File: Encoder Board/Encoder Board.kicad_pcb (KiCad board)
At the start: 2 copper layers, 16 parts, among them J1 Conn_02x05_Odd_Even, J2 Conn_02x05_Odd_Even, J3 Conn_01x02_Pin, U1 AM26LV32xD, U2 AM26LV31xD_1

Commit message: Layout
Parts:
- J3: footprint Connector_PinHeader_1.00mm:PinHeader_1x02_P1.00mm_Horizontal -> Connector_PinHeader_2.00mm:PinHeader_1x02_P2.00mm_Vertical
- moved C1 60.5 mm to (90.8, 48.0)
- moved GND_1 45.0 mm to (84.2, 82.8)
- moved +5V_1 43.4 mm to (88.6, 67.0)
- moved NT1 39.3 mm to (118.2, 59.4), turned to 180 degrees
- moved J2 26.7 mm to (125.7, 56.0)
- moved J3 26.4 mm to (126.0, 73.8), turned to 180 degrees
- moved U2 25.7 mm to (124.5, 83.6), turned to 0 degrees
- moved J1 21.5 mm to (81.7, 69.2)
- moved C2 13.6 mm to (129.6, 80.4), turned to -90 degrees
- moved +3V3_1 12.9 mm to (122.2, 67.6)
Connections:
- R1 pad 1: /B_N -> /A_N
- R1 pad 2: /B -> /A
- R2 pad 1: /A_N -> /B_N
- R2 pad 2: /A -> /B
- U1 pad 1: /B_N -> /A_N
- U1 pad 2: /B -> /A
- U1 pad 6: /A -> /B
- U1 pad 7: /A_N -> /B_N
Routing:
- net +3V3: track 0.00 -> 85.9 mm, vias 0 -> 2
- net /A_N: track 8.81 -> 86.1 mm, vias 0 -> 2
- net +5V: track 0.00 -> 65.9 mm, vias 0 -> 2
- net /A: track 13.3 -> 76.8 mm, vias 0 -> 2
- net /B_N: track 10.5 -> 68.6 mm, vias 0 -> 2
- net /INDEX_N: track 23.8 -> 81.0 mm, vias 0 -> 2
- net /INDEX: track 32.5 -> 87.0 mm, vias 0 -> 2
- net /B: track 14.9 -> 67.0 mm, vias 0 -> 2
- net /B_3V3: track 0.00 -> 14.5 mm
- net /A_3V3: track 0.00 -> 14.5 mm
- net GND: track 0.00 -> 13.7 mm, vias 0 -> 4
- net /TRIGGER_P: track 0.00 -> 12.0 mm
- net /TRIGGER_N: track 0.00 -> 10.7 mm
- net /INDEX_3V3: track 0.00 -> 9.39 mm
- net /TRIGGER: track 0.00 -> 8.46 mm
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- added copper zone on B.Cu, net GND
- added copper zone on F.Cu, net GND
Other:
- board outline added: 56.8 x 55.6 mm

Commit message: Update 2x5 connector footprint
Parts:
- J1, J2: footprint Connector_Molex_Milligrid:Molex_8783210xx_2x05_P2.0mm_Header_Vertical -> Connector_PinHeader_2.54mm:PinHeader_2x05_P2.54mm_Vertical
- moved J2 5.70 mm to (127.9, 61.3), turned to 180 degrees
- moved J1 4.36 mm to (83.9, 73.0), turned to 180 degrees
- moved +5V_1 1.61 mm to (88.4, 65.4)
- moved GND_1 0.45 mm to (83.8, 82.6)
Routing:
- net GND: track 13.7 -> 9.45 mm, vias 4 -> 2
- net /A_N: track 86.1 -> 83.1 mm, vias 2 -> 0
- net /INDEX: track 87.0 -> 84.3 mm, vias 2 -> 0
- net +5V: track 65.9 -> 63.3 mm, vias 2 -> 1
- net /B_N: track 68.6 -> 66.3 mm, vias 2 -> 0
- net /INDEX_N: track 81.0 -> 78.9 mm, vias 2 -> 0
- net /B: track 67.0 -> 66.5 mm, vias 2 -> 0
- net /A: track 76.8 -> 76.7 mm, vias 2 -> 0

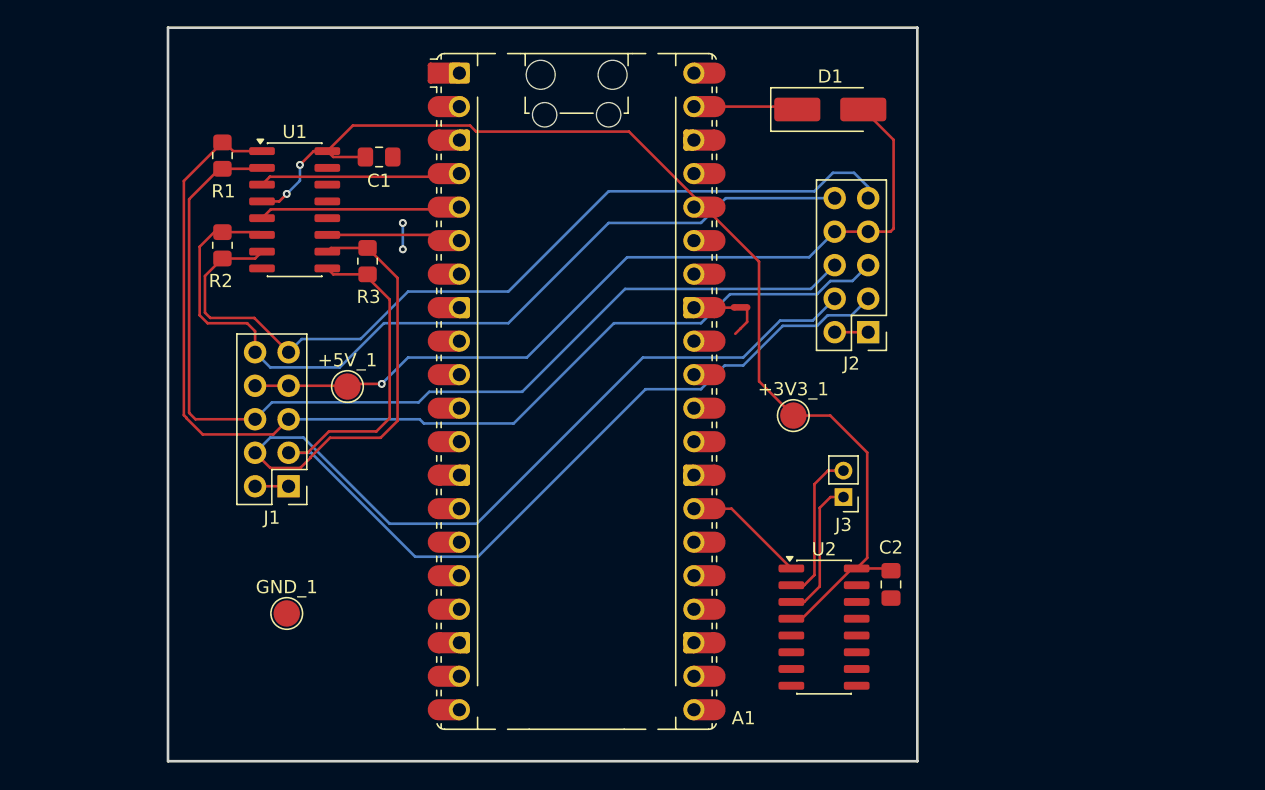
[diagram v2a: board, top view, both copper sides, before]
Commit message: Update layout with new passives
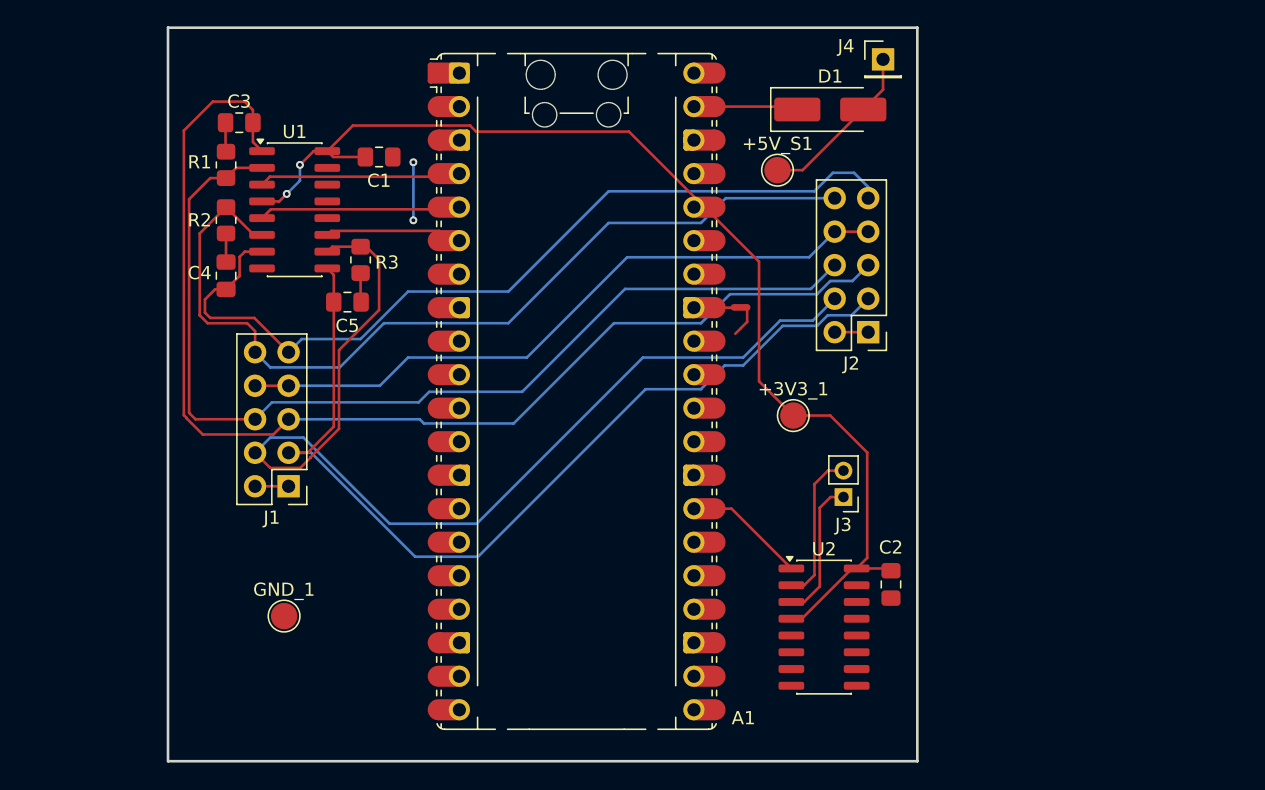
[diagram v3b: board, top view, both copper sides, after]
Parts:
- added C3: 0.0047mF, Capacitor_SMD:C_0805_2012Metric_Pad1.18x1.45mm_HandSolder, F.Cu at (80.2, 45.4)
- added C4: 0.0047mF, Capacitor_SMD:C_0805_2012Metric_Pad1.18x1.45mm_HandSolder, F.Cu at (79.2, 57.0)
- added C5: 0.0047mF, Capacitor_SMD:C_0805_2012Metric_Pad1.18x1.45mm_HandSolder, F.Cu at (88.4, 59.0)
- added J4: Conn_01x01_Pin, Connector_PinHeader_2.54mm:PinHeader_1x01_P2.54mm_Vertical, F.Cu at (129.0, 40.6)
- R1, R2, R3: value 120 -> 110
- moved +5V_S1 36.5 mm to (121.0, 49.0)
- moved R2 1.91 mm to (79.2, 52.8)
- moved R1 0.76 mm to (79.2, 48.6)
- moved R3 0.53 mm to (89.4, 55.8)
- moved GND_1 0.28 mm to (83.6, 82.8)
- renumbered +5V_1 to +5V_S1
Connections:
- +5V_S1 pad 1: +5V -> +5V_S
- D1 pad 2: +5V -> +5V_S
- J1 pad 7: +5V -> +5V_E
- J1 pad 8: +5V -> +5V_E
- J2 pad 7: +5V -> +5V_E
- J2 pad 8: +5V -> +5V_E
- R1 pad 1: /A_N -> Net-(C3-Pad2)
- R2 pad 1: /B_N -> Net-(C4-Pad2)
- R3 pad 1: /INDEX_N -> Net-(C5-Pad2)
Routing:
- net +5V: track 63.3 -> 0.00 mm, vias 1 -> 0
- net +5V_E: track 0.00 -> 51.3 mm
- net +5V_S: track 0.00 -> 12.8 mm
- net /INDEX_N: track 78.9 -> 71.7 mm
- net /A_N: track 83.1 -> 90.2 mm
- net /INDEX: track 84.3 -> 80.8 mm
- net Net-(C5-Pad2): track 0.00 -> 2.45 mm
- net GND: track 9.45 -> 11.9 mm
- net Net-(C3-Pad2): track 0.00 -> 2.27 mm
- net Net-(C4-Pad2): track 0.00 -> 2.16 mm
- net /B: track 66.5 -> 68.6 mm

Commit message: remove differential trigger
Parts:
- removed C2: 0.1u, Capacitor_SMD:C_0805_2012Metric_Pad1.18x1.45mm_HandSolder
- removed U2: AM26LV31xD_1, Package_SO:SOIC-16_3.9x9.9mm_P1.27mm
- J3: value Conn_01x02_Pin -> Conn_01x01_Pin; footprint Connector_PinHeader_2.00mm:PinHeader_1x02_P2.00mm_Vertical -> Connector_PinHeader_2.54mm:PinHeader_1x01_P2.54mm_Vertical
- moved +3V3_1 39.9 mm to (89.2, 45.2)
- moved J3 2.54 mm to (128.4, 74.6), turned to 0 degrees
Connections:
- J3 pad 1: /TRIGGER_N -> /TRIGGER
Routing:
- net +3V3: track 85.9 -> 42.0 mm
- net /TRIGGER_P: track 12.0 -> 0.00 mm
- net /TRIGGER_N: track 10.7 -> 0.00 mm
- net /TRIGGER: track 8.46 -> 13.0 mm

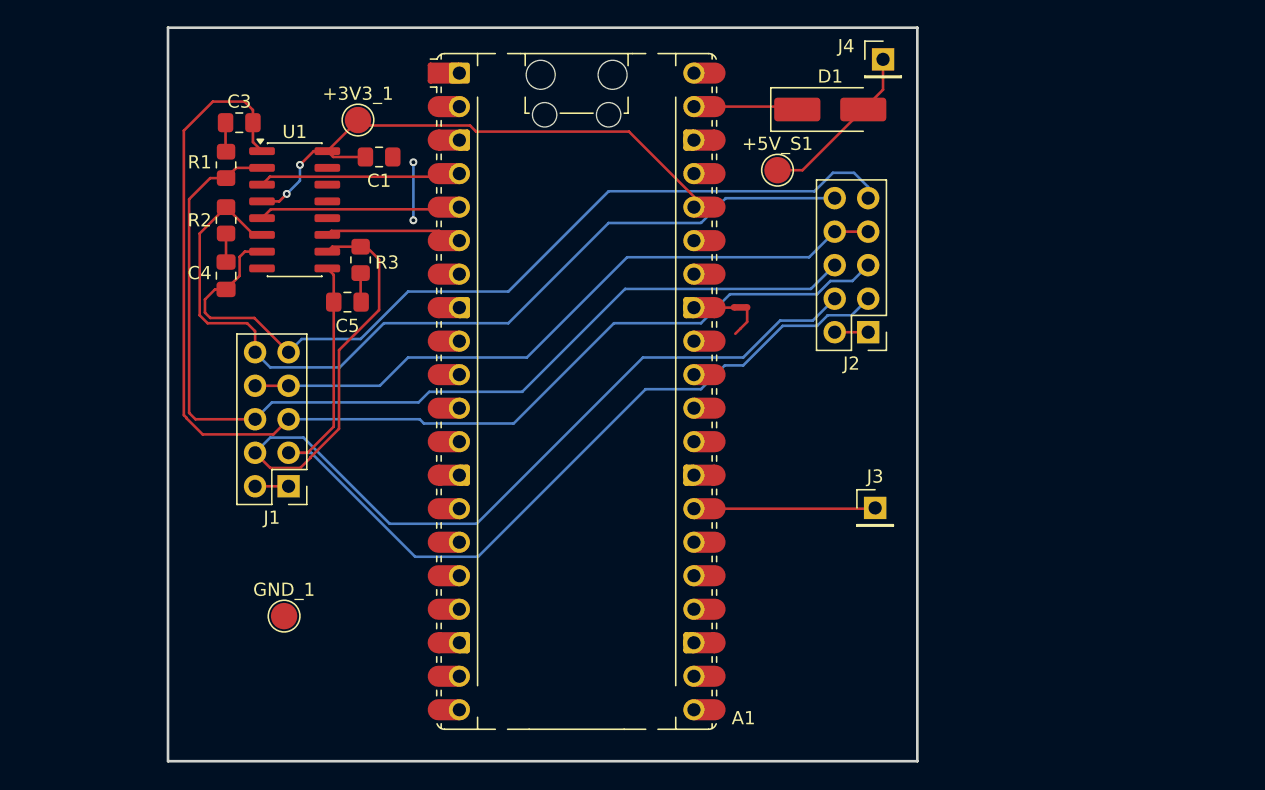
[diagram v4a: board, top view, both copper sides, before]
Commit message: Place & route components to optimize board size
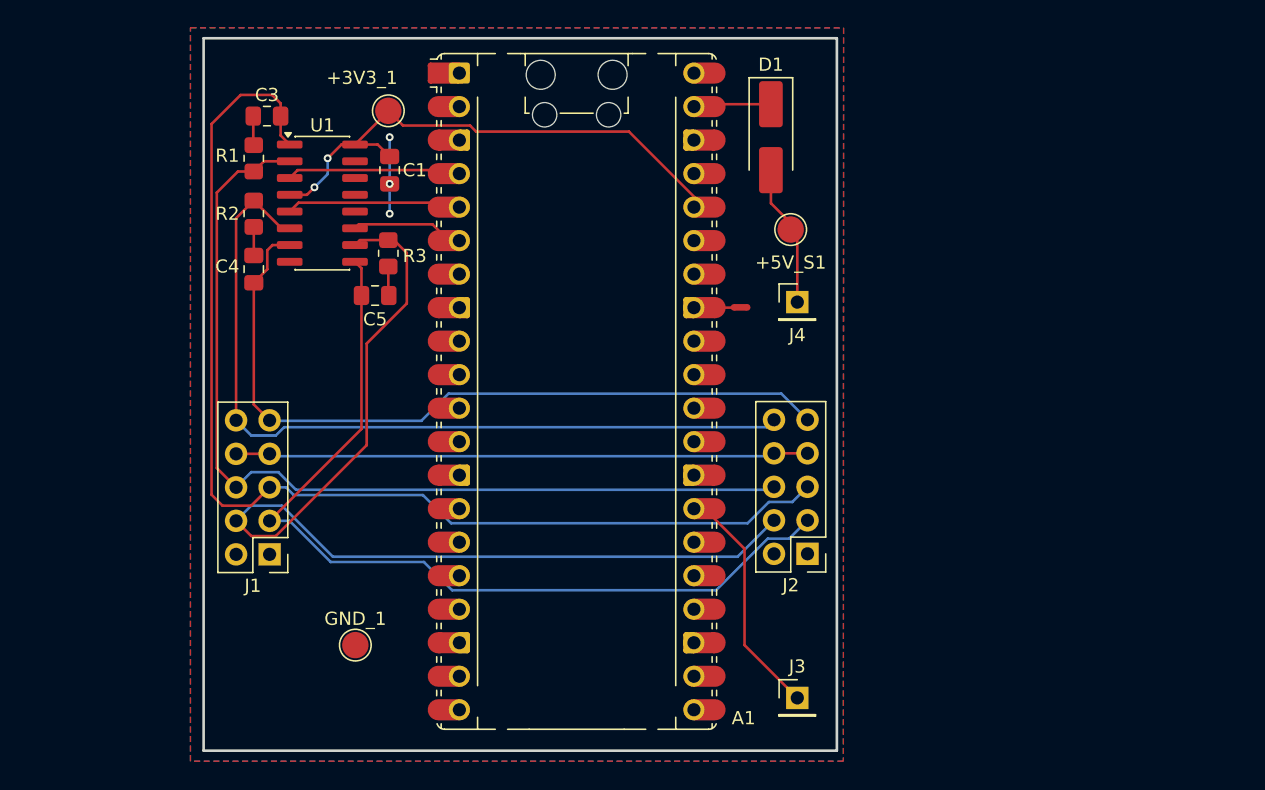
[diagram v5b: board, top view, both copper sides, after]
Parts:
- moved J4 19.5 mm to (122.5, 59.0)
- moved J2 17.4 mm to (123.3, 78.1)
- moved J3 15.6 mm to (122.5, 89.0)
- moved GND_1 5.83 mm to (89.0, 85.0)
- moved J1 5.36 mm to (82.5, 78.1)
- moved D1 4.97 mm to (120.5, 46.5), turned to -90 degrees
- moved +5V_S1 4.61 mm to (122.0, 53.5)
- moved +3V3_1 2.40 mm to (91.5, 44.5)
- moved C3 2.16 mm to (82.3, 44.9)
- moved C4 2.16 mm to (81.3, 56.5)
- moved C5 2.16 mm to (90.5, 58.5)
- moved R1 2.16 mm to (81.3, 48.1)
- moved R2 2.16 mm to (81.3, 52.3)
- moved R3 2.16 mm to (91.5, 55.3)
- moved U1 2.16 mm to (86.5, 51.5)
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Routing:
- net +5V_E: track 51.3 -> 43.5 mm
- net /B_N: track 66.1 -> 58.4 mm
- net /B: track 68.6 -> 62.6 mm
- net GND: track 11.9 -> 5.80 mm, vias 2 -> 3
- net /A: track 76.8 -> 71.5 mm
- net /TRIGGER: track 13.0 -> 17.3 mm
- net /INDEX_N: track 71.7 -> 67.9 mm
- net /INDEX: track 80.8 -> 77.5 mm
- net /A_N: track 90.2 -> 87.0 mm
- net /A_3V3: track 14.5 -> 12.4 mm
- net +3V3: track 42.0 -> 40.0 mm
- net /B_3V3: track 14.5 -> 12.5 mm
- net Net-(A1-VSYS): track 7.13 -> 5.11 mm
- net +5V_S: track 12.8 -> 10.8 mm
- net /INDEX_3V3: track 9.64 -> 8.18 mm
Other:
- board size 56.8 x 55.6 mm -> 48 x 54 mm

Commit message: Update DRC from PCBWay
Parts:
- +3V3_1, +5V_S1, GND_1: footprint TestPoint:TestPoint_Pad_D2.0mm -> TestPoints_WideSM:TestPoint_Pad_D2.0mm_WideSM
- moved J4 1.00 mm to (122.5, 60.0)
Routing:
- net +5V_S: track 10.8 -> 11.8 mm
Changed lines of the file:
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@@
 		(0 "F.Cu" signal)
 		(2 "B.Cu" signal)
-		(9 "F.Adhes" user "F.Adhesive")
-		(11 "B.Adhes" user "B.Adhesive")
 		(13 "F.Paste" user)
 		(15 "B.Paste" user)
@@
 		(1 "F.Mask" user)
 		(3 "B.Mask" user)
-		(17 "Dwgs.User" user "User.Drawings")
-		(19 "Cmts.User" user "User.Comments")
-		(21 "Eco1.User" user "User.Eco1")
-		(23 "Eco2.User" user "User.Eco2")
 		(25 "Edge.Cuts" user)
 		(27 "Margin" user)
@@
 		(35 "F.Fab" user)
 		(33 "B.Fab" user)
-		(39 "User.1" user)
-		(41 "User.2" user)
-		(43 "User.3" user)
-		(45 "User.4" user)
 	)
 	(setup
+		(stackup
+			(layer "F.SilkS"
+				(type "Top Silk Screen")
+			)
+			(layer "F.Paste"
+				(type "Top Solder Paste")
+			)
+			(layer "F.Mask"
+				(type "Top Solder Mask")
+				(thickness 0.01)
+			)
+			(layer "F.Cu"
+				(type "copper")
+				(thickness 0.035)
+			)
+			(layer "dielectric 1"
+				(type "core")
+				(thickness 1.51)
+				(material "FR4")
+				(epsilon_r 4.5)
+				(loss_tangent 0.02)
+			)
+			(layer "B.Cu"
+				(type "copper")
+				(thickness 0.035)
+			)
+			(layer "B.Mask"
+				(type "Bottom Solder Mask")
+				(thickness 0.01)
+			)
+			(layer "B.Paste"
+				(type "Bottom Solder Paste")
+			)
+			(layer "B.SilkS"
+				(type "Bottom Silk Screen")
+			)
+			(copper_finish "None")
+			(dielectric_constraints no)
+		)
 		(pad_to_mask_clearance 0)
+		(solder_mask_min_width 0.1016)
 		(allow_soldermask_bridges_in_footprints no)
 		(tenting
@@
 	(footprint "Connector_PinHeader_2.54mm:PinHeader_1x01_P2.54mm_Vertical"
 		(layer "F.Cu")
-		(at 122.5 59)
+		(at 122.5 60)
 		(descr "Through hole straight pin header, 1x01, 2.54mm pitch, single row")
 		(tags "Through hole pin header THT 1x01 2.54mm single row")
@@
 		)
 	)
-	(footprint "TestPoint:TestPoint_Pad_D2.0mm"
+	(footprint "TestPoints_WideSM:TestPoint_Pad_D2.0mm_WideSM"
 		(layer "F.Cu")
 		(at 91.5 44.5)
@@
 		(tags "test point SMD pad")
 		(property "Reference" "+3V3_1"
-			(at -2 -2.5 0)
+			(at -1 -2.5 0)
 			(layer "F.SilkS")
 			(effects
@@
 		(fp_circle
 			(center 0 0)
-			(end 0 1.2)
+			(end 1.3 0)
 			(stroke
 				(width 0.12)
@@
 		)
 	)
-	(footprint "TestPoint:TestPoint_Pad_D2.0mm"
+	(footprint "TestPoints_WideSM:TestPoint_Pad_D2.0mm_WideSM"
 		(layer "F.Cu")
 		(at 89 85)
@@
 		(tags "test point SMD pad")
 		(property "Reference" "GND_1"
-			(at 0 -1.998 0)
+			(at 0 2.5 0)
 			(layer "F.SilkS")
 			(effects
@@
 		(fp_circle
 			(center 0 0)
-			(end 0 1.2)
+			(end 1.3 0)
 			(stroke
 				(width 0.12)
@@
 		(tags "capacitor handsolder")
 		(property "Reference" "C1"
-			(at 0 -1.9 180)
+			(at 2.5 0.1 180)
 			(layer "F.SilkS")
 			(effects
@@
 		)
 	)
-	(footprint "TestPoint:TestPoint_Pad_D2.0mm"
+	(footprint "TestPoints_WideSM:TestPoint_Pad_D2.0mm_WideSM"
 		(layer "F.Cu")
 		(at 122 53.5)
@@
 		(fp_circle
 			(center 0 0)
-			(end 0 1.2)
+			(end 1.3 0)
 			(stroke
 				(width 0.12)
@@
 	)
 	(segment
-		(start 122.5 59)
+		(start 122 53.5)
 		(end 122.5 54)
 		(width 0.2)
@@
 	)
 	(segment
-		(start 122.5 54)
-		(end 122 53.5)
+		(start 122 53.5)
+		(end 122 53)
 		(width 0.2)
 		(layer "F.Cu")
@@
 	)
 	(segment
-		(start 122 53.5)
-		(end 122 53)
+		(start 120.5 51.5)
+		(end 120.5 49)
 		(width 0.2)
 		(layer "F.Cu")
@@
 	)
 	(segment
-		(start 120.5 51.5)
-		(end 120.5 49)
+		(start 122.5 54)
+		(end 122.5 60)
 		(width 0.2)
 		(layer "F.Cu")
@@
 	)
 	(segment
-		(start 91.5 44.5)
-		(end 92.615 45.615)
+		(start 108.729779 46.079)
+		(end 108.733779 46.075)
+		(width 0.2)
+		(layer "F.Cu")
+		(net "+3V3")
+	)
+	(segment
+		(start 92.5 45.5)
+		(end 97.57918 45.5)
 		(width 0.2)
 		(layer "F.Cu")
@@
 	)
 	(segment
+		(start 103.883779 46.075)
+		(end 107.666221 46.075)
+		(width 0.2)
+		(layer "F.Cu")
+		(net "+3V3")
+	)
+	(segment
 		(start 91.6 47.9625)
 		(end 90.6925 47.055)
@@
 	)
 	(segment
-		(start 97.69418 45.615)
+		(start 97.57918 45.5)
 		(end 98.15418 46.075)
 		(width 0.2)
@@
 	)
 	(segment
-		(start 115.465 51.8)
+		(start 108.733779 46.075)
 		(end 109.74 46.075)
 		(width 0.2)
@@
 	)
 	(segment
-		(start 109.74 46.075)
-		(end 98.15418 46.075)
+		(start 98.15418 46.075)
+		(end 102.816221 46.075)
 		(width 0.2)
 		(layer "F.Cu")
@@
 	)
 	(segment
-		(start 84.025 50.865)
-		(end 85.335 50.865)
+		(start 107.670221 46.079)
+		(end 108.729779 46.079)
 		(width 0.2)
 		(layer "F.Cu")
@@
 	)
 	(segment
-		(start 92.615 45.615)
-		(end 97.69418 45.615)
+		(start 84.025 50.865)
+		(end 85.335 50.865)
 		(width 0.2)
 		(layer "F.Cu")
@@
 		(width 0.2)
 		(layer "F.Cu")
+		(net "+3V3")
+	)
+	(segment
+		(start 102.820221 46.079)
+		(end 103.879779 46.079)
+		(width 0.2)
+		(layer "F.Cu")
+		(net "+3V3")
+	)
+	(segment
+		(start 109.74 46.075)
+		(end 115.465 51.8)
+		(width 0.2)
+		(layer "F.Cu")
+		(net "+3V3")
+	)
+	(segment
+		(start 107.666221 46.075)
+		(end 107.670221 46.079)
+		(width 0.2)
+		(layer "F.Cu")
+		(net "+3V3")
+	)
+	(segment
+		(start 91.5 44.5)
+		(end 92.5 45.5)
+		(width 0.2)
+		(layer "F.Cu")
+		(net "+3V3")
+	)
+	(segment
+		(start 103.879779 46.079)
+		(end 103.883779 46.075)
+		(width 0.2)
+		(layer "F.Cu")
+		(net "+3V3")
+	)
+	(segment
+		(start 102.816221 46.075)
+		(end 102.820221 46.079)
+		(width 0.2)
+		(layer "F.Cu")
